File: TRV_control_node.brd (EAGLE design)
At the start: 65 x 30.7 mm, 48 parts, among them J1 AMP FCI 10103594-0001LF, J3 USB-MICROB, J4 455-1750-1-ND, J6 AMP FCI 10103594-0001LF, Q6 BSS84W-7-F, SW1 EVQQ, SW2 EVQQ, U1 PCA9306, U11 915MHz, U2 FT231XQ-R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

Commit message: schematic changes
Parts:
- removed J2: (no value), SparkFun-Connectors:1X04
- removed Q6: BSS84W-7-F, MOSFETs:SOT323
- removed R13, R6: 10K, Adafruit Feather 32u4 Bluefruit LE:MICROBUILDER__0402MP
- removed R21: 10M, Adafruit Feather 32u4 Bluefruit LE:MICROBUILDER__0402MP
- added C3: 100uF, adafruit:C1210
- added C7: 0.1uF, Adafruit Feather 32u4 Bluefruit LE:MICROBUILDER__0402MP
- added J5: AMP FCI 10103594-0001LF, SparkFun-Connectors:USB-MICROB-PTH
- added U$1: OLED_091_SSD1306, oled_096_SSD1306:OLED_128X32_0.91
- J3: value USB-MICROB -> AMP FCI 10103594-0001LF; device SparkFun-Connectors:USB-MICROB@1 -> SparkFun-Connectors:USB-MICROB-PTH
- moved J1 59.8 mm to (62.0, 19.2), turned to 90 degrees
- moved R5 49.3 mm to (33.0, 12.5)
- moved J3 43.5 mm to (3.00, 11.0), turned to 270 degrees
- moved R9 42.2 mm to (43.0, 0.80), turned to 180 degrees
- moved R15 41.7 mm to (7.60, 20.4)
- moved R3 41.2 mm to (31.2, 0.60), turned to 180 degrees
- moved C6 39.9 mm to (7.60, 21.3), turned to 180 degrees
- moved R11 39.5 mm to (7.60, 19.5), turned to 180 degrees
- moved C12 39.1 mm to (33.0, 11.3)
- moved C5 39.0 mm to (36.6, 5.90), turned to 270 degrees
- moved STAT 37.2 mm to (34.7, 1.10), turned to 270 degrees
- moved C15 32.2 mm to (28.8, 7.40), turned to 270 degrees
- moved U2 24.8 mm to (35.9, 18.2)
- moved R8 19.5 mm to (25.5, -22.2)
- moved C2 11.7 mm to (58.3, 33.2), turned to 180 degrees
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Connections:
- removed net 5.0V: RPI1.2, RPI1.4, RPI1.S2, RPI1.S4
- removed net D+: J6.D+
- removed net D-: J6.D-
- removed net FTDI_RX: R20.1
- removed net GND1: J6.GND
- removed net VBAT: Q6.3
- new net 5VA: C6.2, D2.A, J1.VBUS, J6.VBUS, RPI1.2, RPI1.4, RPI1.S2, RPI1.S4, U2.VCC
- net 3.3V: no longer RPI1.1, RPI1.17, RPI1.S1, RPI1.S17
- net 3.3VB: now also RPI1.1, RPI1.17, RPI1.S1, RPI1.S17, U$1.P$2
- net 5VB: now also C3.1, C7.2, J3.VBUS, J4.3, J5.VBUS
- net CH0: now also J4.2
- net GND: now also C3.2, C7.1, J4.1, J5.GND, J6.GND, U$1.P$1; no longer J3.MT1, J3.MT2, R21.1
- net N$32: now also J1.D-, J6.D-; no longer J3.D-
- net N$33: now also J1.D+, J6.D+; no longer J3.D+
- net RX: now also RPI1.8, RPI1.S8
- net SCL: now also U$1.P$3; no longer R13.1
- net SDA: now also U$1.P$4; no longer R6.1
- net TX: now also R20.1, RPI1.10, RPI1.S10
- net VBUS: no longer C6.2, D2.A, J1.VBUS, J3.VBUS, J6.VBUS, Q6.1, R21.2, U2.VCC
- net VCC: no longer R13.2, R6.2
- net VIN: no longer Q6.2

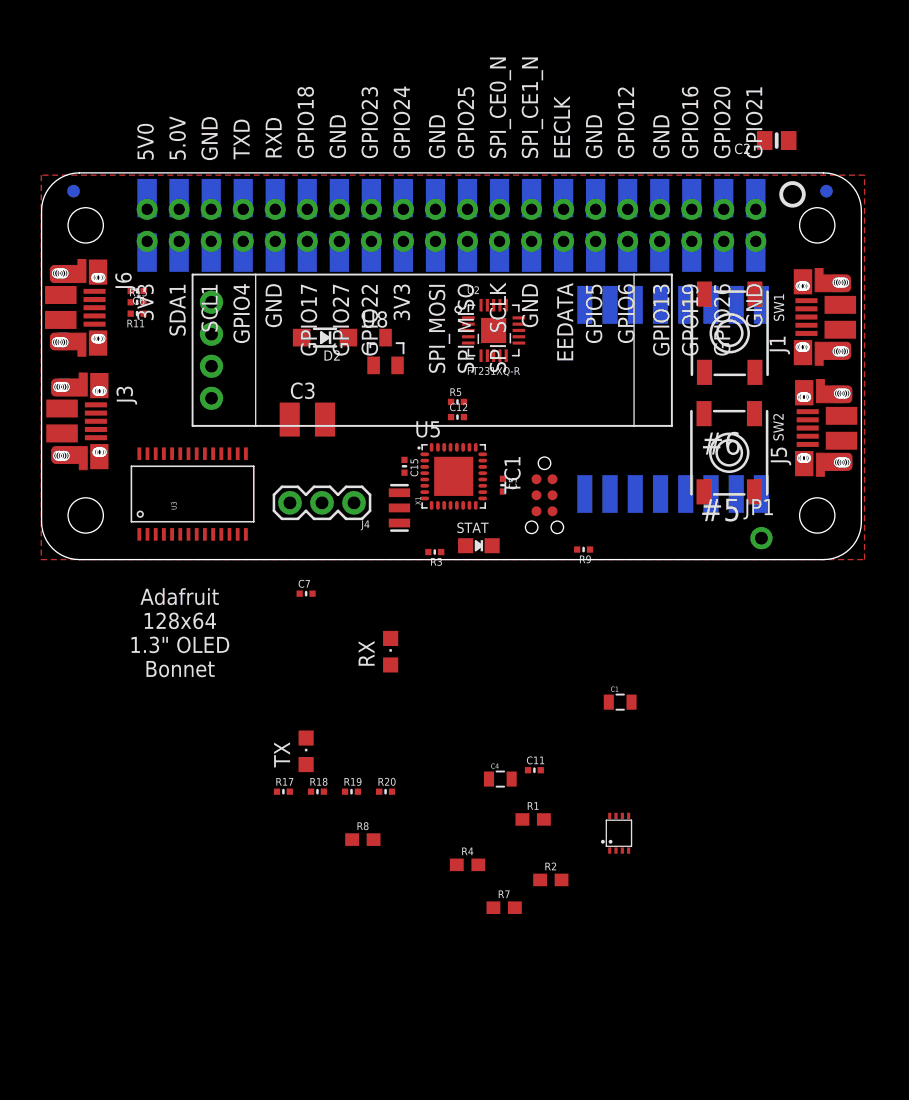
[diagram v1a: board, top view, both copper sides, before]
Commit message: Arranged components on brd
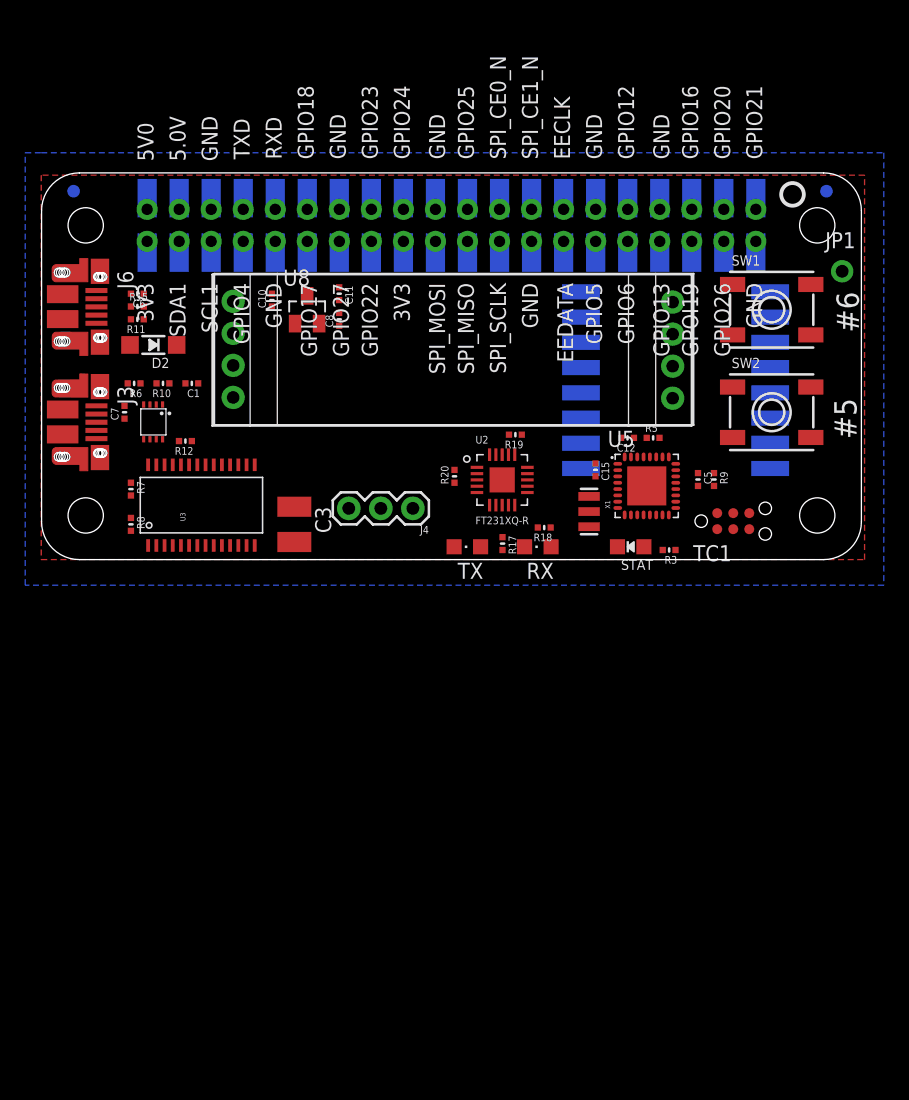
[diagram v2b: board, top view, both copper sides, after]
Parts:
- removed C2: 10uF, microbuilder:0805-NO
- removed C4: 10uF, SparkFun-Capacitors:0805
- removed J1, J5: AMP FCI 10103594-0001LF, SparkFun-Connectors:USB-MICROB-PTH
- removed R1, R2: 10k, SparkFun-Resistors:0603
- removed R4: 200k, SparkFun-Resistors:0603
- added C10: 1uF, Adafruit Feather 32u4 Bluefruit LE:MICROBUILDER__0402MP
- added C8: 10uF, Adafruit Feather 32u4 Bluefruit LE:MICROBUILDER__0402MP
- added R10, R6: 10K, Adafruit Feather 32u4 Bluefruit LE:MICROBUILDER__0402MP
- added R12: 200K, Adafruit Feather 32u4 Bluefruit LE:MICROBUILDER__0402MP
- added U$3: OLED_091_SSD1306, oled_096_SSD1306:OLED_128X32_0.91
- C1: value 1uF -> 10uF; device SparkFun-Capacitors:0805 -> Adafruit Feather 32u4 Bluefruit LE:MICROBUILDER__0402MP
- R7, R8: value 10k -> 10K; device SparkFun-Resistors:0603 -> Adafruit Feather 32u4 Bluefruit LE:MICROBUILDER__0402MP
- moved U1 49.3 mm to (8.89, 10.9), turned to 180 degrees
- moved R7 44.5 mm to (7.11, 5.59), turned to 270 degrees
- moved C1 42.3 mm to (11.9, 14.0), turned to 180 degrees
- moved C11 40.8 mm to (23.6, 21.1), turned to 270 degrees
- moved R19 31.1 mm to (37.6, 9.91), turned to 180 degrees
- moved R8 31.0 mm to (7.11, 2.79), turned to 270 degrees
- moved R18 27.6 mm to (39.9, 2.54), turned to 180 degrees
- moved R17 26.2 mm to (36.6, 1.27), turned to 270 degrees
- moved R20 25.6 mm to (32.8, 6.60), turned to 90 degrees
- moved JP1 22.1 mm to (63.5, 22.9)
- moved TX 20.6 mm to (33.8, 1.02), turned to 90 degrees
- moved C7 20.4 mm to (6.60, 11.7), turned to 90 degrees
- moved R3 18.6 mm to (49.8, 0.76)
- moved R5 15.8 mm to (48.5, 9.65)
- moved C5 15.5 mm to (52.1, 6.35)
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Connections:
- removed net 3.3V: C2.1
- net 3.3VB: now also C1.2, R10.1, R6.1; no longer R7.2, R8.2
- net 5VA: no longer J1.VBUS
- net 5VB: now also R12.1, R7.1, R8.1; no longer J5.VBUS, R1.2, R2.2, R4.2
- net GND: now also C1.1, C10.1, C8.1; no longer C1.2, C2.2, C4.2, J1.GND, J5.GND
- net LV_SCL: now also R10.2; no longer R7.1
- net LV_SDA: now also R6.2; no longer R8.1
- net N$1: now also R12.2; no longer R4.1
- net N$32: no longer J1.D-
- net N$33: no longer J1.D+
- net N$6: now also R8.2; no longer R2.1
- net N$7: now also R7.2; no longer R1.1
- net SCL: no longer U5.28
- net SDA: no longer U5.27
- net VCC: now also C8.2; no longer C4.1
- net VIN: now also C10.2; no longer C1.1
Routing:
- added copper zone on layer 16, net GND
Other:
- board text added: "Designed by Akram Ali"
- board text added: "TRV Control Node v0.4.0 June 2018"
- board text removed: "Adafruit 128x64 1.3" OLED Bonnet"

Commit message: Completed routing
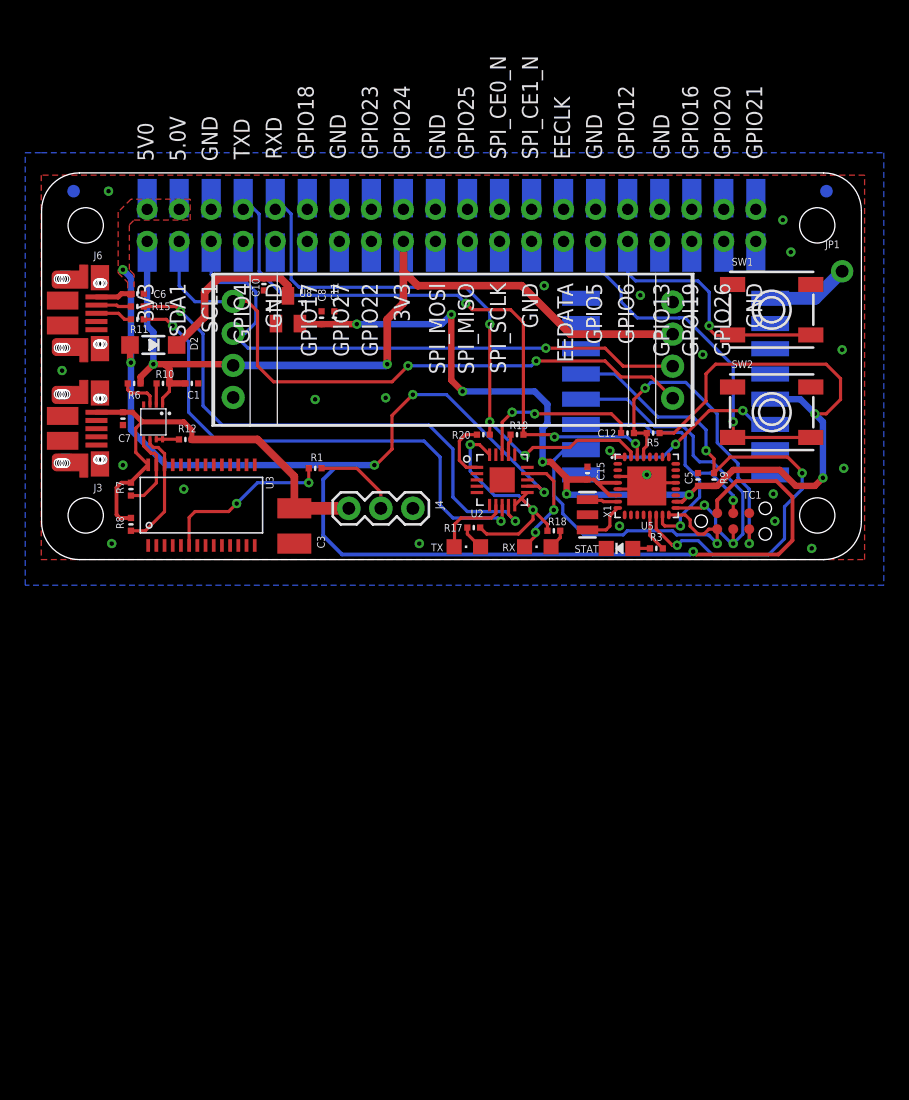
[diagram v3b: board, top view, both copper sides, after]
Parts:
- removed U$2: (no value), microbuilder:PCBFEAT-REV-040
- added R1: 220, Adafruit Feather 32u4 Bluefruit LE:MICROBUILDER__0402MP
- D2: value SOD123 -> STPS140Z
- U8: value MCP1703CB -> MCP1703/3.3V
- moved R20 4.02 mm to (35.1, 9.91), turned to 180 degrees
- moved R17 2.62 mm to (34.3, 2.54), turned to 180 degrees
- moved C11 1.94 mm to (23.2, 19.2)
- moved U8 1.52 mm to (19.6, 19.8)
- moved C10 1.42 mm to (17.7, 21.8)
- moved C8 1.40 mm to (22.2, 19.2), turned to 270 degrees
- moved R3 1.02 mm to (48.8, 0.89), turned to 0 degrees
- moved STAT 0.90 mm to (45.8, 0.89)
- moved R18 0.80 mm to (40.6, 2.29)
- moved C15 0.68 mm to (43.3, 6.86)
- moved C7 0.52 mm to (6.48, 11.2)
- moved J3 0.51 mm to (3.05, 10.4)
- moved U11 0.51 mm to (50.3, 13.7)
- moved J6 0.51 mm to (3.05, 19.6)
- moved C12 0.38 mm to (46.5, 10.0)
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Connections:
- removed net A0: U5.23
- removed net A1: U5.24
- removed net A2: U5.25
- removed net A3: U5.26
- removed net A6: U5.19
- removed net A7: U5.22
- removed net CH1: U3.7
- removed net CH10: U3.17
- removed net CH11: U3.18
- removed net CH12: U3.19
- removed net CH13: U3.20
- removed net CH14: U3.21
- removed net CH15: U3.22
- removed net CH2: U3.8
- removed net CH3: U3.9
- removed net CH4: U3.10
- removed net CH5: U3.11
- removed net CH6: U3.12
- removed net CH7: U3.13
- removed net CH8: U3.15
- removed net CH9: U3.16
- removed net D3: U5.1
- removed net D4: U5.2
- removed net D5: U5.9
- removed net D6: U5.10
- removed net D7: U5.11
- removed net D8: U5.12
- removed net GPIO17: RPI1.11, RPI1.S11
- removed net GPIO22: RPI1.15, RPI1.S15
- removed net GPIO23: RPI1.16, RPI1.S16
- removed net GPIO27: RPI1.13, RPI1.S13
- removed net GPIO4: RPI1.7, RPI1.S7
- removed net VBUS: TC1.2
- new net N$9: R1.2, U3.6
- net 3.3VB: now also U$3.P$2
- net 5VA: now also TC1.2
- net CH0: now also R1.1; no longer U3.6
- net GND: now also U$3.P$1
- net SCL: now also U$3.P$3
- net SDA: now also U$3.P$4
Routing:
- net 5VA: track 0.00 -> 117.7 mm, vias 0 -> 6
- net VCC: track 0.00 -> 95.8 mm, vias 0 -> 8
- net 3.3VB: track 0.00 -> 69.9 mm, vias 0 -> 2
- net SDA: track 0.00 -> 50.3 mm, vias 0 -> 2
- net RX: track 0.00 -> 49.0 mm, vias 0 -> 3
- net TX: track 0.00 -> 48.0 mm, vias 0 -> 3
- net SCL: track 0.00 -> 47.3 mm, vias 0 -> 1
- net N$25: track 0.00 -> 43.6 mm, vias 0 -> 2
- net SS: track 0.00 -> 42.3 mm, vias 0 -> 3
- net N$26: track 0.00 -> 41.8 mm, vias 0 -> 2
- net 5VB: track 0.00 -> 35.8 mm
- net SCK: track 0.00 -> 28.7 mm, vias 0 -> 2
- net GPIO5: track 0.00 -> 28.5 mm, vias 0 -> 1
- net MISO: track 0.00 -> 26.6 mm, vias 0 -> 1
- net RESET: track 0.00 -> 26.4 mm, vias 0 -> 2
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- added copper zone on layer 1, net 5VA
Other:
- board text removed: "#5"
- board text removed: "#6"

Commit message: Adjustments
- Removed second OLED screen pins
- Moved USB ports slightly away from each other
- Silkscreen adjustments
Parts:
- removed U$3: OLED_091_SSD1306, oled_096_SSD1306:OLED_128X32_0.91
- moved C7 0.38 mm to (6.48, 10.8)
- moved J3 0.38 mm to (3.05, 10.0)
- moved J6 0.38 mm to (3.05, 19.9)
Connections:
- net 3.3VB: no longer U$3.P$2
- net GND: no longer U$3.P$1
- net SCL: no longer U$3.P$3
- net SDA: no longer U$3.P$4
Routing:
- net SDA: track 50.3 -> 8.34 mm, vias 2 -> 0
- net SCL: track 47.3 -> 11.3 mm, vias 1 -> 0
- net 3.3VB: track 69.9 -> 46.5 mm
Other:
- board text added: "RPi"
- board text added: "Servo"

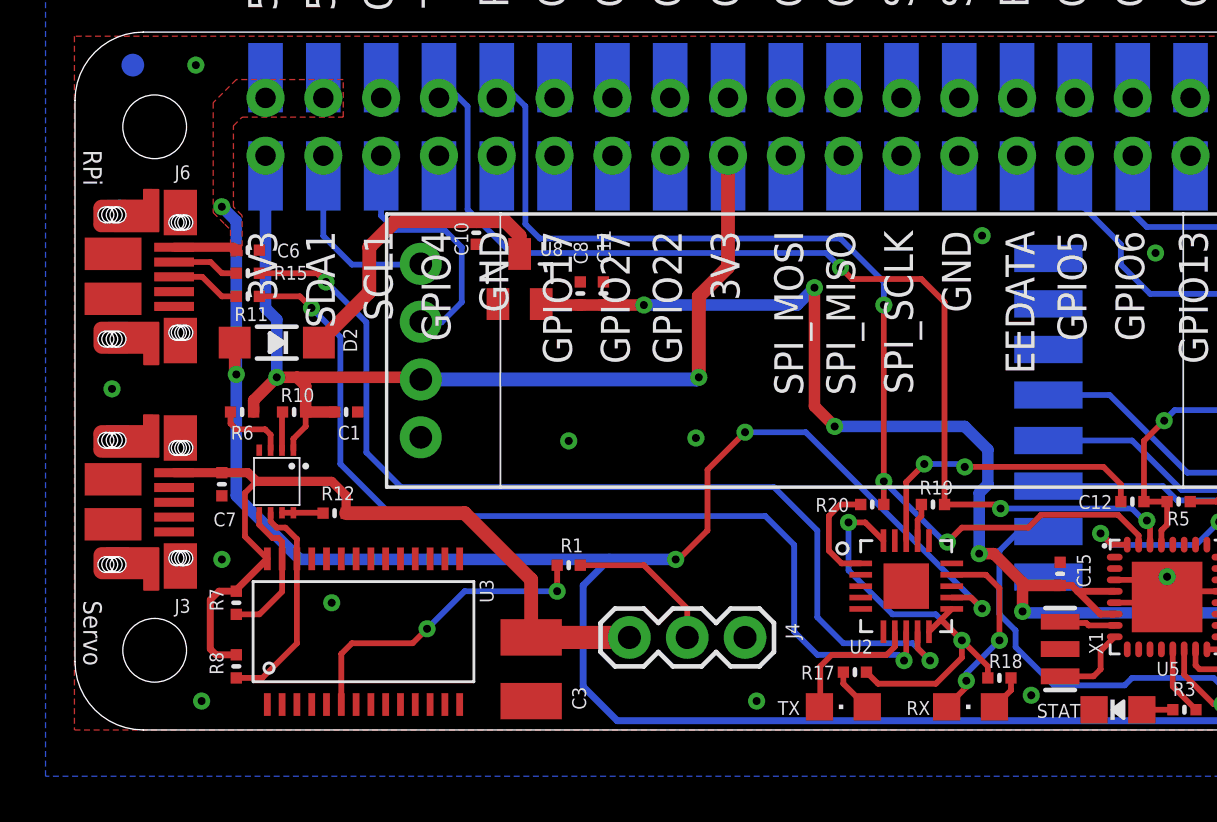
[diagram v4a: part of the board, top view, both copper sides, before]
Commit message: USB ports adjustment
- Moved USB ports a bit further away
- Some trace adjustments
- ERC and DRC
- Some silkscreen adjustments
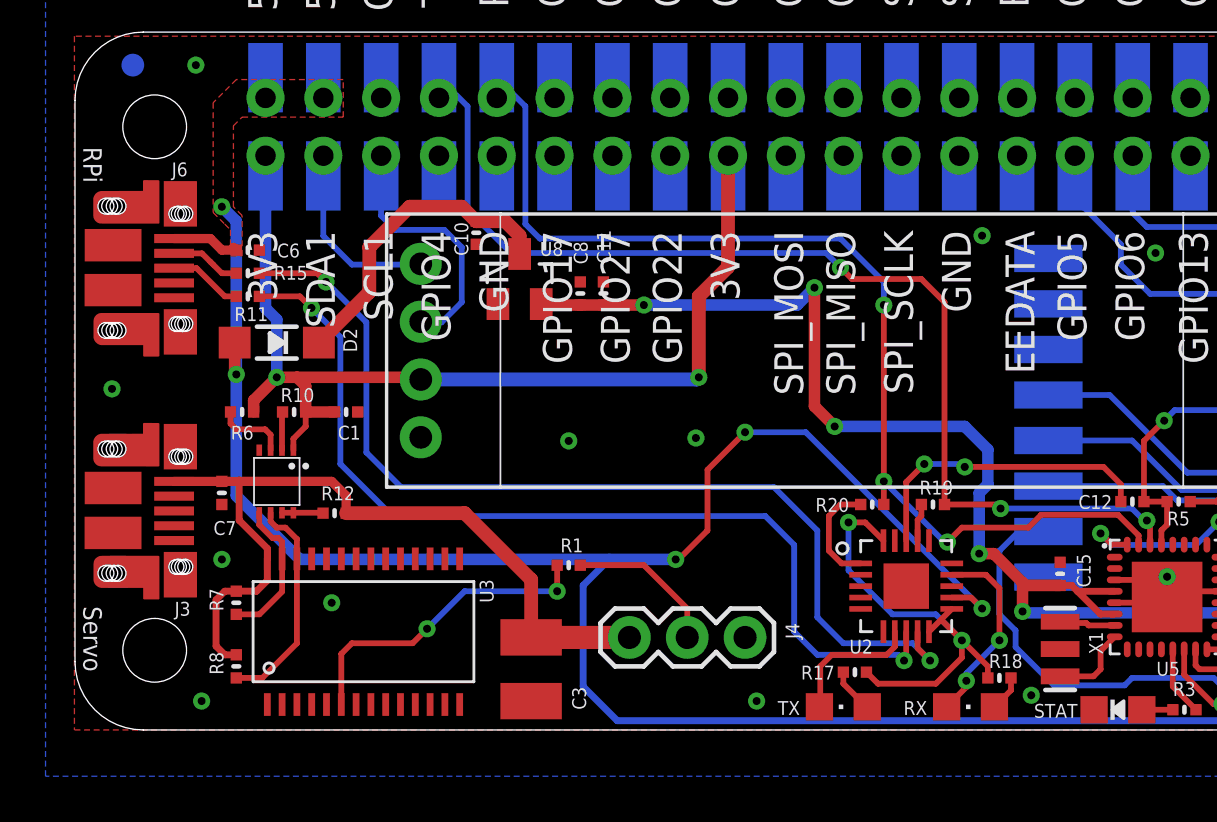
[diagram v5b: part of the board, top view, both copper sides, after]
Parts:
- moved C7 0.38 mm to (6.48, 10.4)
- moved J3 0.38 mm to (3.05, 9.65)
- moved J6 0.38 mm to (3.05, 20.3)
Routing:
- net VIN: track 13.3 -> 13.8 mm
